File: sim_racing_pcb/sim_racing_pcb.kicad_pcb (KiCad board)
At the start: 2 copper layers, 100 x 50 mm, 21 parts, among them J1 Conn_02x04_Socket, U1 A1302KUA-T, U2 A1302KUA-T, U3 LM358, U4 LM1117MP-3.3, U5 LM7805_TO220, U6 Pico

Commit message: codigo de relleno usb lib en C
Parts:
- removed C1, C2: 10uF, Capacitor_THT:CP_Radial_D5.0mm_P2.50mm
- removed C3: 0.33uF, Capacitor_THT:C_Disc_D3.0mm_W2.0mm_P2.50mm
- removed C4: 0.1uF, Capacitor_THT:C_Disc_D3.0mm_W2.0mm_P2.50mm
- removed R10, R4, R5: 10k, Resistor_THT:R_Axial_DIN0207_L6.3mm_D2.5mm_P10.16mm_Horizontal
- removed R2, R8: 2,2k, Resistor_THT:R_Axial_DIN0207_L6.3mm_D2.5mm_P10.16mm_Horizontal
- removed R3, R7, R9: 1k, Resistor_THT:R_Axial_DIN0207_L6.3mm_D2.5mm_P10.16mm_Horizontal
- removed R6: 4,7k, Resistor_THT:R_Axial_DIN0207_L6.3mm_D2.5mm_P10.16mm_Horizontal
- removed U1, U2: A1302KUA-T, Connector_PinHeader_2.54mm:PinHeader_1x03_P2.54mm_Vertical
- removed U3: LM358, Package_DIP:DIP-8_W10.16mm_LongPads
- removed U4: LM1117MP-3.3, Package_TO_SOT_SMD:SOT-223-3_TabPin2
- removed U5: LM7805_TO220, Package_TO_SOT_THT:TO-220-3_Vertical
- added H1: MountingHole, MountingHole:MountingHole_4.3mm_M4_DIN965, F.Cu at (105.0, 24.0)
- added H2: MountingHole, MountingHole:MountingHole_4.3mm_M4_DIN965, F.Cu at (195.0, 24.0)
- added H3: MountingHole, MountingHole:MountingHole_4.3mm_M4_DIN965, F.Cu at (105.0, 66.0)
- added H4: MountingHole, MountingHole:MountingHole_4.3mm_M4_DIN965, F.Cu at (195.0, 66.0)
- added J10: AS5600_POW, Connector_PinHeader_2.54mm:PinHeader_1x03_P2.54mm_Vertical, F.Cu at (167.0, 23.1)
- added J11: Conn_01x08_Pin, Connector_PinHeader_2.54mm:PinHeader_1x08_P2.54mm_Vertical, F.Cu at (114.2, 63.1)
- added J12: Conn_01x02_Pin, Connector_PinHeader_2.54mm:PinHeader_1x02_P2.54mm_Vertical, F.Cu at (186.8, 44.7)
- added J13: Conn_01x02_Pin, Connector_PinHeader_2.54mm:PinHeader_1x02_P2.54mm_Vertical, F.Cu at (113.3, 24.7)
- added J2: Paddle_Shift_R, Connector_Molex:Molex_SL_171971-0002_1x02_P2.54mm_Vertical, F.Cu at (186.8, 56.8)
- added J3: Paddle_Shift_L, Connector_Molex:Molex_SL_171971-0002_1x02_P2.54mm_Vertical, F.Cu at (109.9, 54.2)
- added J4: Conn_02x04_Odd_Even, Connector_PinHeader_2.54mm:PinHeader_2x04_P2.54mm_Vertical, F.Cu at (145.5, 65.0)
- added J5: Leds, Connector_PinHeader_2.54mm:PinHeader_1x03_P2.54mm_Vertical, F.Cu at (121.3, 27.2)
- added J6: AS5600, Connector_PinHeader_2.54mm:PinHeader_1x05_P2.54mm_Vertical, F.Cu at (161.3, 25.6)
- added J8: Encoder - DER, Connector_PinHeader_2.54mm:PinHeader_1x05_P2.54mm_Vertical, F.Cu at (173.2, 24.5)
- added J9: Encoder - MID, Connector_PinHeader_2.54mm:PinHeader_1x05_P2.54mm_Vertical, F.Cu at (180.2, 64.8)
- J1: value Conn_02x04_Socket -> Pedales MicroUsb; footprint Connector_PinHeader_2.54mm:PinHeader_2x04_P2.54mm_Vertical -> Connector_PinHeader_2.54mm:PinHeader_1x05_P2.54mm_Vertical
- R1: value 1k -> 330
- moved J1 112.1 mm to (135.2, 25.6)
- moved R1 91.6 mm to (142.8, 30.1), turned to 180 degrees
- moved U6 88.5 mm to (141.5, 45.3)
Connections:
- J1 pad 1: +5V -> +3V3
- J1 pad 2: +3V3 -> A1-Brk
- J1 pad 3: DIR -> A0-Acc
- J1 pad 4: SDA -> unconnected-(J1-Pin_4-Pad4)
- J1 pad 5: SCL -> GND
- R1 pad 1: Hall_1 -> LEDS
- U6 pad 1: unconnected-(U6-GPIO0-Pad1) -> Shifter_mec_L
- U6 pad 10: unconnected-(U6-GPIO7-Pad10) -> DIS - LED
- U6 pad 11: unconnected-(U6-GPIO8-Pad11) -> DIS - DC
- U6 pad 12: unconnected-(U6-GPIO9-Pad12) -> BTN 1
- U6 pad 13: unconnected-(U6-GND-Pad13) -> GND
- U6 pad 14: unconnected-(U6-GPIO10-Pad14) -> BTN 2
- U6 pad 15: unconnected-(U6-GPIO11-Pad15) -> BTN 3
- U6 pad 16: unconnected-(U6-GPIO12-Pad16) -> BTN 4
- U6 pad 17: unconnected-(U6-GPIO13-Pad17) -> CLK - MID
- U6 pad 18: unconnected-(U6-GND-Pad18) -> GND
- U6 pad 19: unconnected-(U6-GPIO14-Pad19) -> SW - MID
- U6 pad 2: unconnected-(U6-GPIO1-Pad2) -> DIS - CS
- U6 pad 20: unconnected-(U6-GPIO15-Pad20) -> DT - MID
- U6 pad 21: unconnected-(U6-GPIO16-Pad21) -> SW - DER
- U6 pad 22: unconnected-(U6-GPIO17-Pad22) -> DT - DER
- U6 pad 23: unconnected-(U6-GND-Pad23) -> GND
- U6 pad 24: unconnected-(U6-GPIO18-Pad24) -> CLK - DER
- U6 pad 25: unconnected-(U6-GPIO19-Pad25) -> DIR
- U6 pad 26: unconnected-(U6-GPIO20-Pad26) -> SDA
- U6 pad 27: unconnected-(U6-GPIO21-Pad27) -> SCL
- U6 pad 28: unconnected-(U6-GND-Pad28) -> GND
- U6 pad 29: unconnected-(U6-GPIO22-Pad29) -> LEDS
- U6 pad 3: unconnected-(U6-GND-Pad3) -> GND
- U6 pad 31: unconnected-(U6-GPIO26_ADC0-Pad31) -> A0-Acc
- U6 pad 32: unconnected-(U6-GPIO27_ADC1-Pad32) -> A1-Brk
- U6 pad 33: unconnected-(U6-AGND-Pad33) -> GND
- U6 pad 36: unconnected-(U6-3V3-Pad36) -> +3V3
- U6 pad 38: unconnected-(U6-GND-Pad38) -> GND
- U6 pad 4: unconnected-(U6-GPIO2-Pad4) -> DIS - RST
- U6 pad 40: unconnected-(U6-VBUS-Pad40) -> +5V
- U6 pad 5: unconnected-(U6-GPIO3-Pad5) -> DIS - MOSI
- U6 pad 7: unconnected-(U6-GPIO5-Pad7) -> Shifter_mec_R
- U6 pad 8: unconnected-(U6-GND-Pad8) -> GND
- U6 pad 9: unconnected-(U6-GPIO6-Pad9) -> DIS - CLK
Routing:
- net GND: track 0.00 -> 254.1 mm
- net +3V3: track 0.00 -> 239.1 mm
- net +5V: track 0.00 -> 59.4 mm
- net Shifter_mec_R: track 0.00 -> 58.7 mm
- net CLK - MID: track 0.00 -> 31.7 mm
- net DIS - DC: track 0.00 -> 27.0 mm
- net CLK - DER: track 0.00 -> 23.4 mm
- net DT - DER: track 0.00 -> 20.6 mm
- net SW - DER: track 0.00 -> 19.9 mm
- net SW - MID: track 0.00 -> 17.7 mm
- net DT - MID: track 0.00 -> 17.6 mm
- net DIS - CLK: track 0.00 -> 14.9 mm
- net DIS - LED: track 0.00 -> 14.4 mm
- net Net-(J5-Pin_2): track 0.00 -> 14.0 mm
- net SCL: track 0.00 -> 12.2 mm
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- added copper zone on B.Cu, net GND

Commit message: minor changes to pcb
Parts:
- H1, H2, H3, H4: footprint MountingHole:MountingHole_4.3mm_M4_DIN965 -> MountingHole:MountingHole_3.2mm_M3_DIN965
- J11: value Conn_01x08_Pin -> Display TFT
- J2, J3: footprint Connector_Molex:Molex_SL_171971-0002_1x02_P2.54mm_Vertical -> Connector_Molex:Molex_KK-254_AE-6410-02A_1x02_P2.54mm_Vertical
- R1: footprint Resistor_THT:R_Axial_DIN0207_L6.3mm_D2.5mm_P10.16mm_Horizontal -> Resistor_THT:R_Axial_DIN0207_L6.3mm_D2.5mm_P15.24mm_Horizontal
- moved J9 6.31 mm to (173.9, 65.0)
- moved J1 3.95 mm to (131.2, 25.6)
- moved J5 3.71 mm to (120.7, 23.6), turned to 0 degrees
- moved J2 2.61 mm to (186.8, 54.2), turned to -90 degrees
- moved J3 2.54 mm to (109.9, 56.8), turned to 90 degrees
- moved J11 0.67 mm to (114.8, 63.1)
- moved R1 0.41 mm to (142.3, 30.3)
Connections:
- J1 pad 2: A1-Brk -> A2-Clutch
- J1 pad 3: A0-Acc -> A1-Brk
- J1 pad 4: unconnected-(J1-Pin_4-Pad4) -> A0-Acc
- J2 pad 1: Shifter_mec_R -> GND
- J2 pad 2: GND -> Shifter_mec_R
- J3 pad 1: Shifter_mec_L -> GND
- J3 pad 2: GND -> Shifter_mec_L
- U6 pad 17: CLK - MID -> SW - MID
- U6 pad 19: SW - MID -> DT - MID
- U6 pad 20: DT - MID -> CLK - MID
- U6 pad 34: unconnected-(U6-GPIO28_ADC2-Pad34)_1 -> A2-Clutch
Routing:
- net GND: track 254.1 -> 281.1 mm
- net CLK - MID: track 31.7 -> 14.2 mm
- net A2-Clutch: track 0.00 -> 11.3 mm
- net Net-(J5-Pin_2): track 14.0 -> 8.10 mm
- net DT - MID: track 17.6 -> 14.2 mm
- net +5V: track 59.4 -> 61.8 mm
- net DIS - LED: track 14.4 -> 13.0 mm
- net +3V3: track 239.1 -> 238.0 mm
- net DIS - CLK: track 14.9 -> 13.8 mm
- net LEDS: track 7.35 -> 8.37 mm
- net SW - MID: track 17.7 -> 16.9 mm
- net DIS - DC: track 27.0 -> 26.3 mm
- net A1-Brk: track 10.8 -> 11.5 mm
- net A0-Acc: track 10.8 -> 11.5 mm
- net Shifter_mec_R: track 58.7 -> 58.1 mm

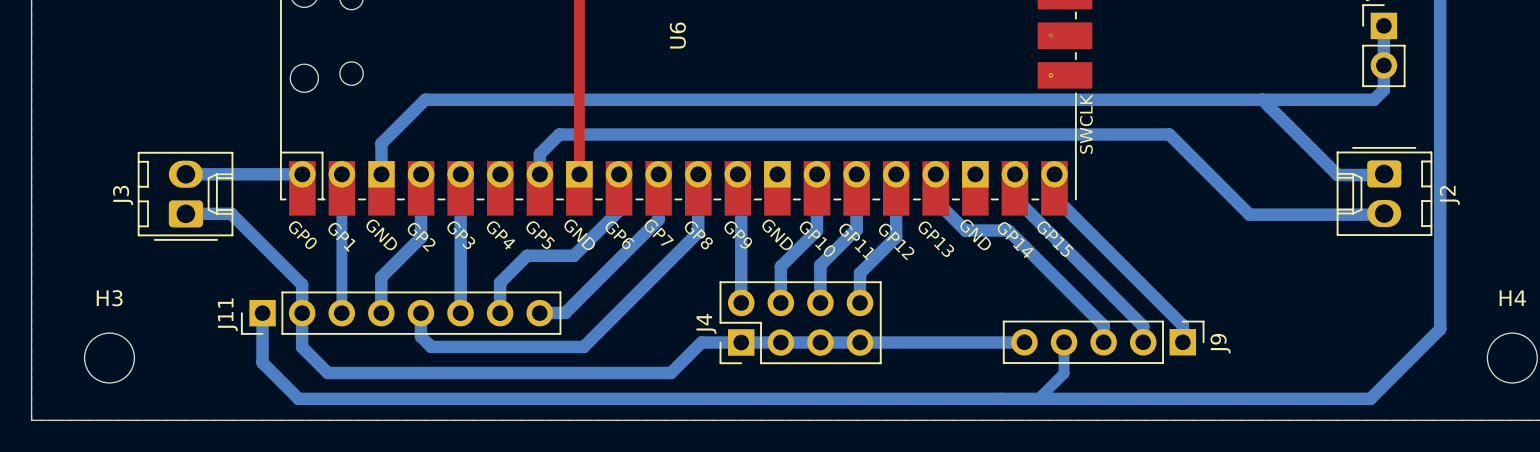
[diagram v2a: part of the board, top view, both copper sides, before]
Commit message: modify pcb display placement
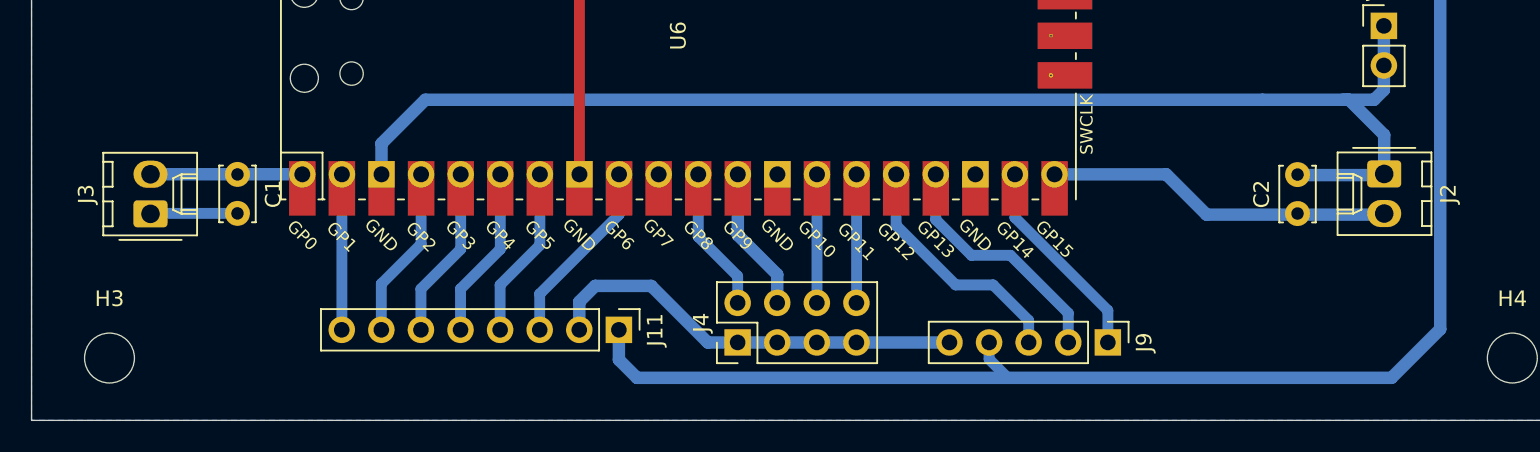
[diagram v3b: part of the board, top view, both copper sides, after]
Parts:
- added C1: 0,1uF, Capacitor_THT:C_Disc_D3.4mm_W2.1mm_P2.50mm, F.Cu at (113.2, 54.2)
- added C2: 0,1uF, Capacitor_THT:C_Disc_D3.4mm_W2.1mm_P2.50mm, F.Cu at (181.2, 56.7)
- J4: value Conn_02x04_Odd_Even -> Buttons
- moved J11 22.9 mm to (137.7, 64.2), turned to -90 degrees
- moved J9 4.81 mm to (169.1, 65.0)
- moved J3 2.27 mm to (107.6, 56.8)
- moved J4 0.23 mm to (145.3, 65.0)
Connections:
- U6 pad 10: DIS - LED -> unconnected-(U6-GPIO7-Pad10)
- U6 pad 11: DIS - DC -> BTN 1
- U6 pad 12: BTN 1 -> BTN 2
- U6 pad 14: BTN 2 -> BTN 3
- U6 pad 15: BTN 3 -> BTN 4
- U6 pad 16: BTN 4 -> SW - MID
- U6 pad 17: SW - MID -> DT - MID
- U6 pad 19: DT - MID -> CLK - MID
- U6 pad 2: DIS - CS -> DIS - LED
- U6 pad 20: CLK - MID -> Shifter_mec_R
- U6 pad 4: DIS - RST -> DIS - CLK
- U6 pad 6: unconnected-(U6-GPIO4-Pad6) -> DIS - DC
- U6 pad 7: Shifter_mec_R -> DIS - RST
- U6 pad 9: DIS - CLK -> DIS - CS
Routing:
- net Shifter_mec_R: track 58.1 -> 22.2 mm
- net +3V3: track 238.0 -> 210.7 mm
- net GND: track 281.1 -> 254.9 mm
- net DIS - DC: track 26.3 -> 11.0 mm
- net DIS - CS: track 8.91 -> 12.1 mm
- net DIS - LED: track 13.0 -> 9.98 mm
- net DIS - CLK: track 13.8 -> 11.0 mm
- net Shifter_mec_L: track 7.50 -> 9.74 mm
- net DIS - MOSI: track 8.91 -> 11.0 mm
- net DT - MID: track 14.2 -> 15.8 mm
- net SW - MID: track 16.9 -> 15.7 mm
- net DIS - RST: track 9.96 -> 11.0 mm
- net BTN 3: track 9.26 -> 8.25 mm
- net BTN 4: track 9.21 -> 8.25 mm
- net BTN 1: track 8.34 -> 9.29 mm
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
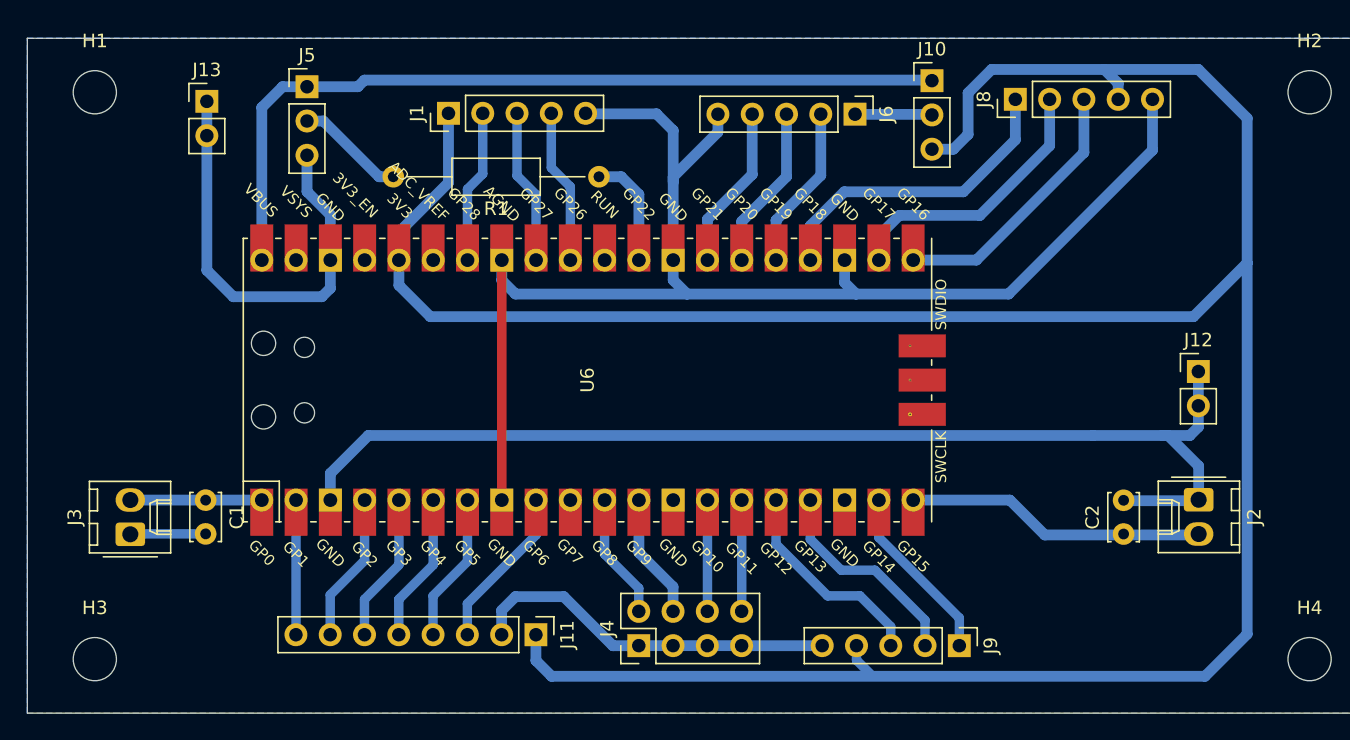
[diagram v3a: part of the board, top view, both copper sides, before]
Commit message: Remove power selection for as5600 and change for molex connectors
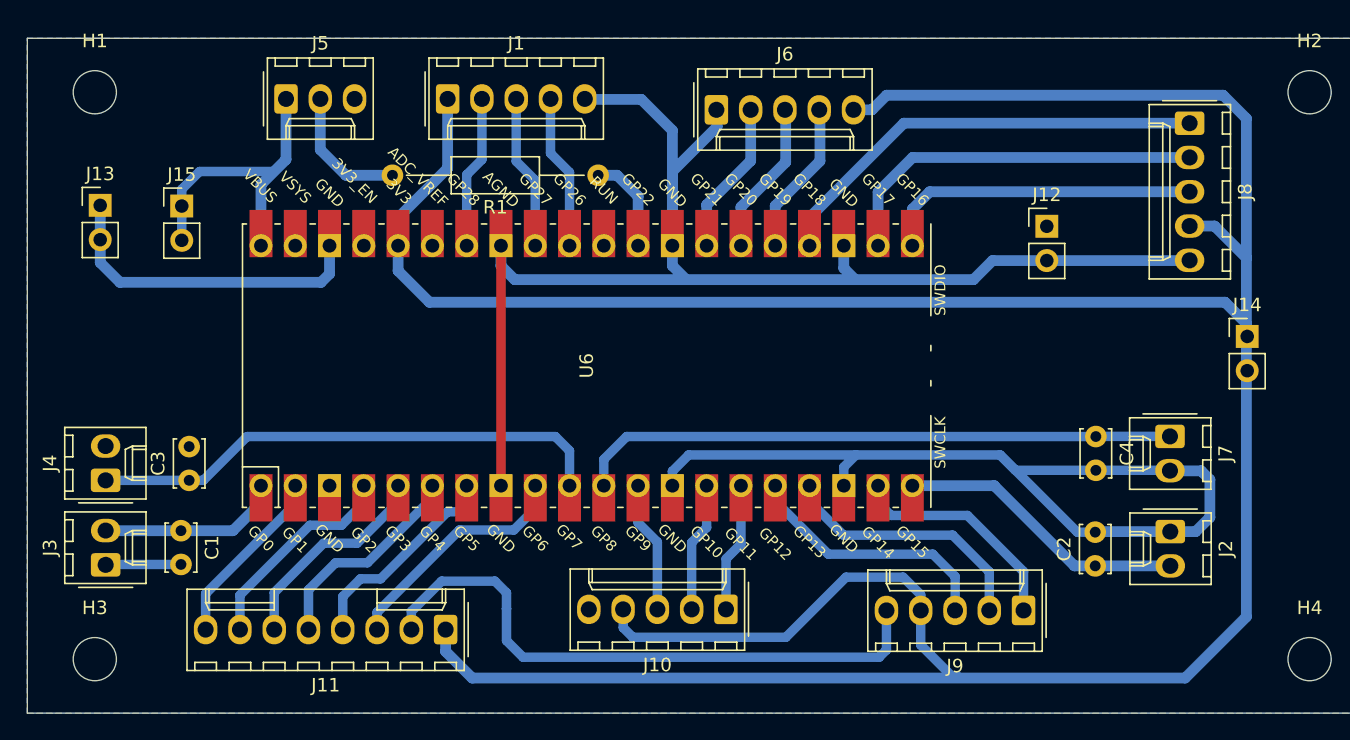
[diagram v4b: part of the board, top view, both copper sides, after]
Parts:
- added C3: 0,1uF, Capacitor_THT:C_Disc_D3.4mm_W2.1mm_P2.50mm, F.Cu at (112.0, 52.8)
- added C4: 0,1uF, Capacitor_THT:C_Disc_D3.4mm_W2.1mm_P2.50mm, F.Cu at (179.2, 49.5)
- added J14: 3V3, Connector_PinHeader_2.54mm:PinHeader_1x02_P2.54mm_Vertical, F.Cu at (190.4, 42.1)
- added J15: 5V, Connector_PinHeader_2.54mm:PinHeader_1x02_P2.54mm_Vertical, F.Cu at (111.4, 32.4)
- added J7: BTN 2, Connector_Molex:Molex_KK-254_AE-6410-02A_1x02_P2.54mm_Vertical, F.Cu at (184.7, 49.5)
- J1, J6, J8, J9: footprint Connector_PinHeader_2.54mm:PinHeader_1x05_P2.54mm_Vertical -> Connector_Molex:Molex_KK-254_AE-6410-05A_1x05_P2.54mm_Vertical
- J10: value AS5600_POW -> Encoder - IZQ; footprint Connector_PinHeader_2.54mm:PinHeader_1x03_P2.54mm_Vertical -> Connector_Molex:Molex_KK-254_AE-6410-05A_1x05_P2.54mm_Vertical
- J11: footprint Connector_PinHeader_2.54mm:PinHeader_1x08_P2.54mm_Vertical -> Connector_Molex:Molex_KK-254_AE-6410-08A_1x08_P2.54mm_Vertical
- J12, J13: value Conn_01x02_Pin -> GND
- J4: value Buttons -> BTN 1; footprint Connector_PinHeader_2.54mm:PinHeader_2x04_P2.54mm_Vertical -> Connector_Molex:Molex_KK-254_AE-6410-02A_1x02_P2.54mm_Vertical
- J5: footprint Connector_PinHeader_2.54mm:PinHeader_1x03_P2.54mm_Vertical -> Connector_Molex:Molex_KK-254_AE-6410-03A_1x03_P2.54mm_Vertical
- moved J10 42.0 mm to (151.8, 62.3), turned to 180 degrees
- moved J4 41.4 mm to (105.8, 52.8)
- moved J12 15.6 mm to (175.5, 33.9)
- moved J8 13.0 mm to (186.1, 26.3), turned to -90 degrees
- moved J13 11.0 mm to (105.4, 32.4)
- moved J6 10.3 mm to (151.1, 25.3), turned to 0 degrees
- moved J11 6.70 mm to (131.0, 63.8), turned to 180 degrees
- moved J9 5.43 mm to (173.8, 62.4), turned to 180 degrees
- moved C2 3.16 mm to (179.1, 59.1)
- moved J2 3.16 mm to (184.7, 56.5)
- moved C1 2.91 mm to (111.4, 56.5)
- moved J3 2.91 mm to (105.8, 59.0)
- moved J5 1.80 mm to (119.2, 24.5)
- moved U6 1.07 mm to (141.4, 44.3)
- moved J1 1.07 mm to (131.1, 24.5), turned to 0 degrees
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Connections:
- J10 pad 1: +5V -> CLK - IZQ
- J10 pad 2: AS5600 -> DT - IZQ
- J10 pad 3: +3V3 -> SW - IZQ
- J4 pad 1: GND -> BTN 1
- J4 pad 2: BTN 1 -> GND
- J6 pad 1: AS5600 -> GND
- J6 pad 2: DIR -> SCL
- J6 pad 4: SCL -> DIR
- J6 pad 5: GND -> +3V3
- U6 pad 10: unconnected-(U6-GPIO7-Pad10) -> BTN 1
- U6 pad 11: BTN 1 -> BTN 2
- U6 pad 12: BTN 2 -> SW - IZQ
- U6 pad 14: BTN 3 -> DT - IZQ
- U6 pad 15: BTN 4 -> CLK - IZQ
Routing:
- net +5V: track 61.8 -> 22.8 mm
- net +3V3: track 210.7 -> 249.4 mm
- net BTN 2: track 9.60 -> 44.8 mm
- net BTN 1: track 9.29 -> 38.8 mm
- net SW - IZQ: track 0.00 -> 10.1 mm
- net CLK - DER: track 23.4 -> 33.1 mm
- net DT - IZQ: track 0.00 -> 9.62 mm
- net CLK - IZQ: track 0.00 -> 9.62 mm
- net GND: track 254.9 -> 245.4 mm
- net BTN 4: track 8.25 -> 0.00 mm
- net BTN 3: track 8.25 -> 0.00 mm
- net DT - DER: track 20.6 -> 28.1 mm
- net DIS - CS: track 12.1 -> 17.9 mm
- net AS5600: track 5.72 -> 0.00 mm
- net DIS - MOSI: track 11.0 -> 15.9 mm
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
